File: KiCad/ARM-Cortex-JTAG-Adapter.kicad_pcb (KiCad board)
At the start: 2 copper layers, 36.1 x 30.5 mm, 4 parts, among them J1 I/O, J2 Power

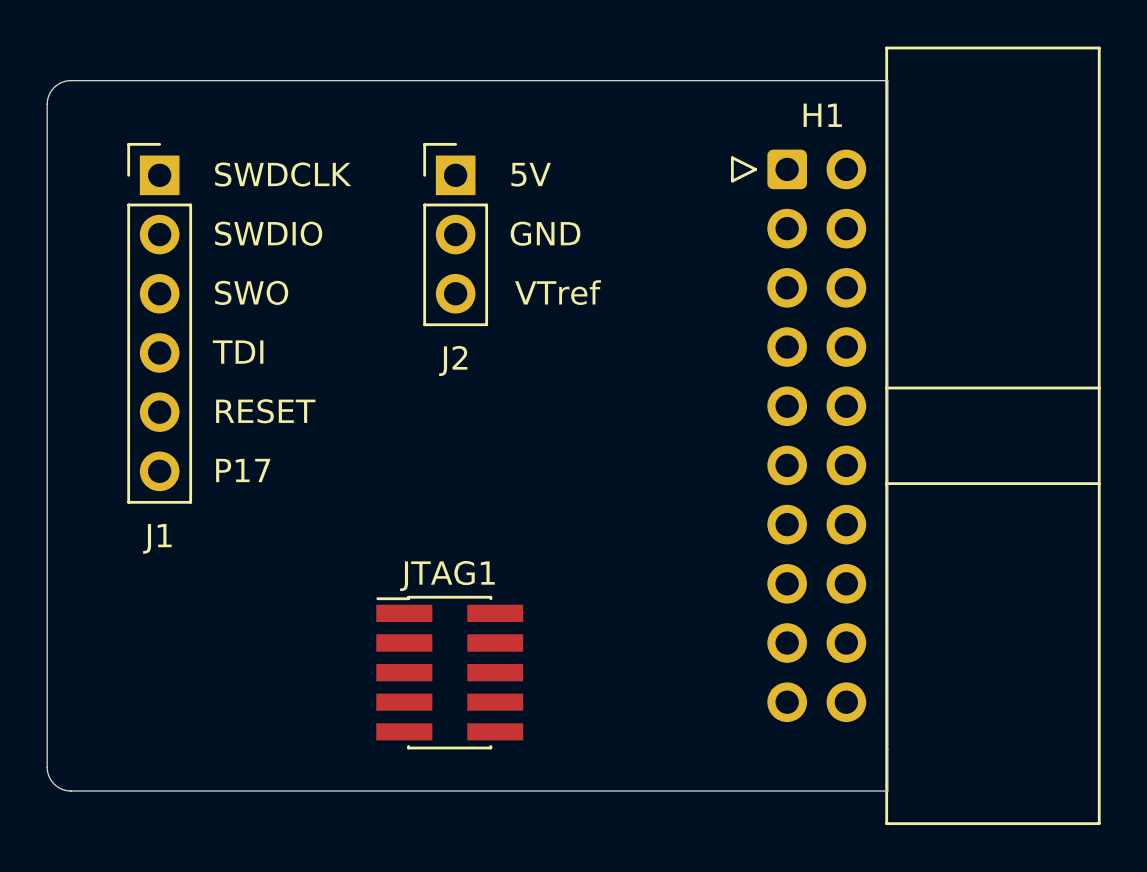
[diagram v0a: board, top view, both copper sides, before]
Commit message: Updating schematic and PCB layout.
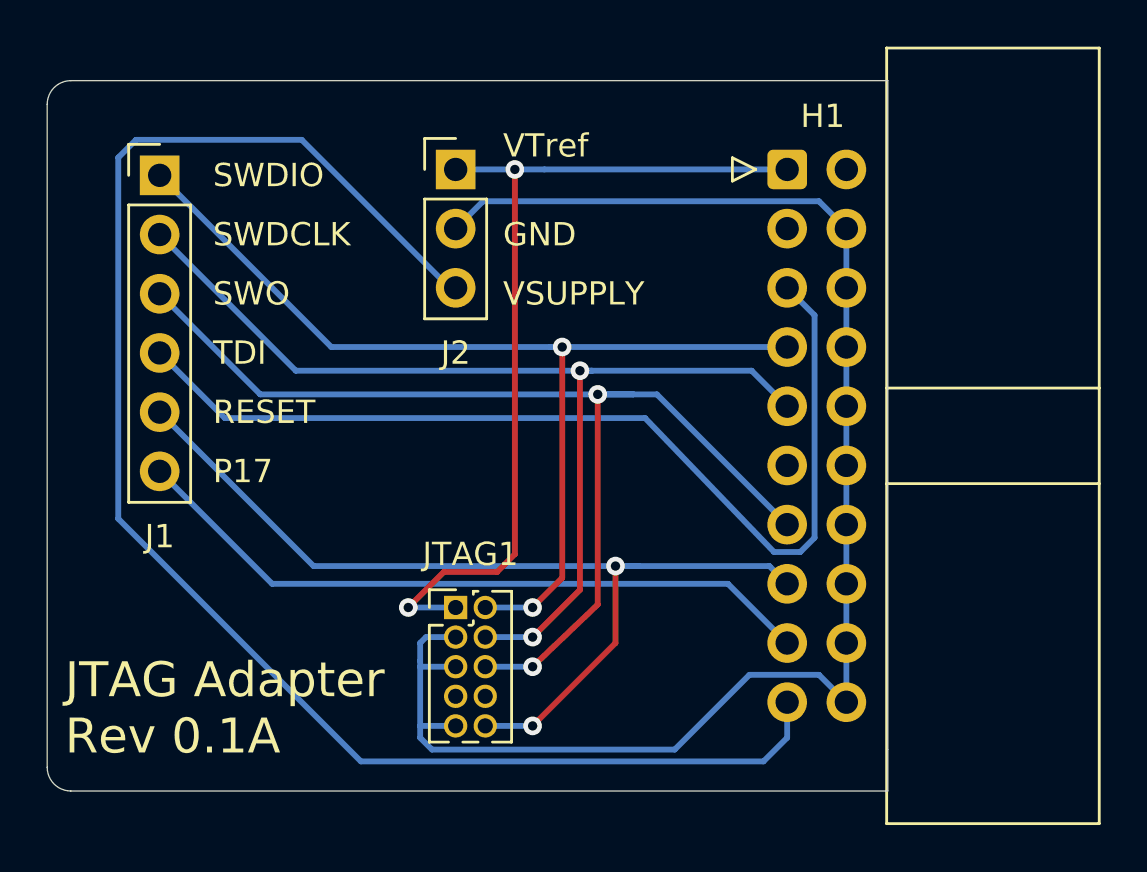
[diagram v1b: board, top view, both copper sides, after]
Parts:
- H1: value 2x10 IDC Header Connector -> IDC-Header_2x10_P2.54mm_Horizontal
- J1: value I/O -> Data
- JTAG1: footprint Connector_PinHeader_1.27mm:PinHeader_2x05_P1.27mm_Vertical_SMD -> Connector_PinHeader_1.27mm:PinHeader_2x05_P1.27mm_Vertical
- moved JTAG1 2.81 mm to (144.8, 129.5)
- moved J2 0.25 mm to (144.8, 110.7)
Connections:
- J1 pad 1: /SWDCLK -> /SWDIO
- J1 pad 2: /SWDIO -> /SWDCLK
- J2 pad 1: /5V -> /VTref
- J2 pad 3: /VTref -> /5V
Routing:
- net /5V: track 0.00 -> 68.0 mm
- net /GND: track 0.00 -> 67.1 mm
- net /SWO: track 0.00 -> 47.5 mm, vias 0 -> 2
- net /SWDCLK: track 0.00 -> 44.8 mm, vias 0 -> 2
- net /SWDIO: track 0.00 -> 43.7 mm, vias 0 -> 2
- net /TDI: track 0.00 -> 43.2 mm
- net /RESET: track 0.00 -> 41.1 mm, vias 0 -> 2
- net /VTref: track 0.00 -> 38.3 mm, vias 0 -> 2
- net /P17: track 0.00 -> 30.0 mm
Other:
- board text added: "JTAG Adapter Rev 0.1A"
- board text added: "VSUPPLY"
- board text removed: "5V"

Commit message: Revising schematic for optional TDI pin.
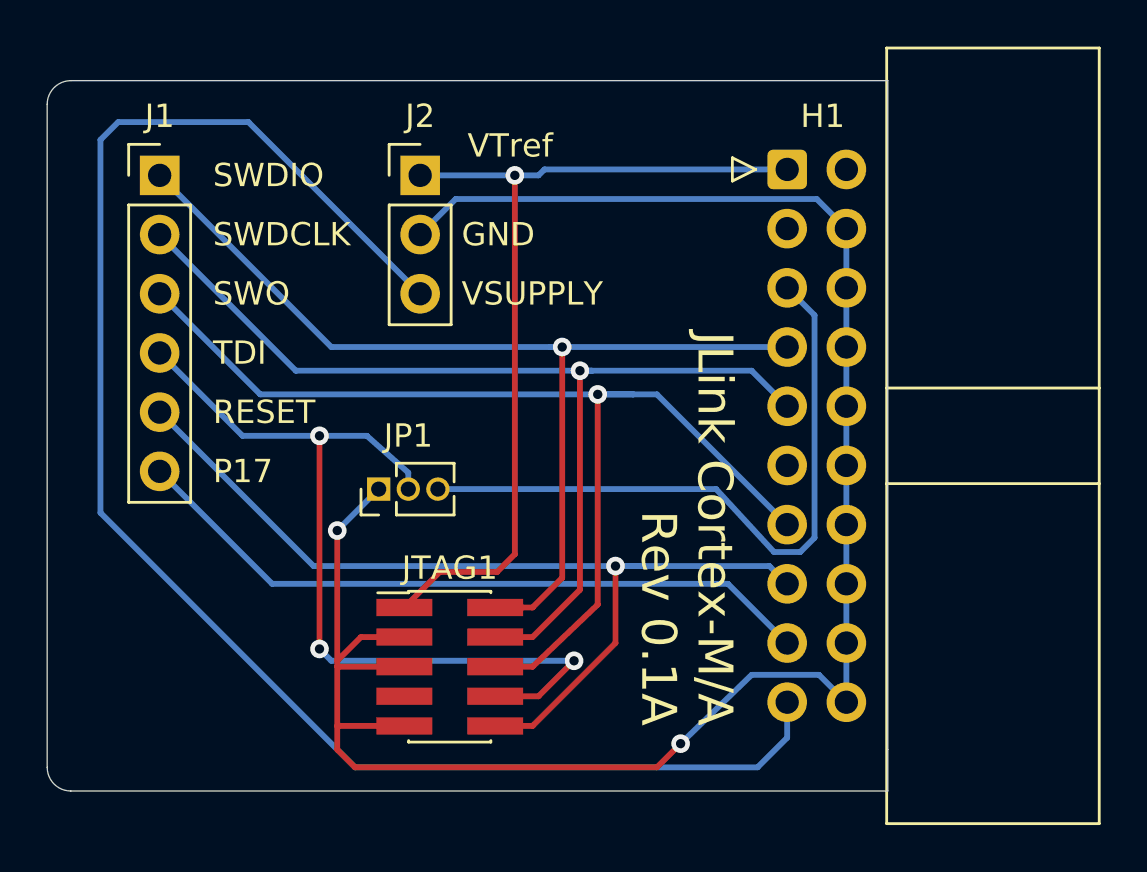
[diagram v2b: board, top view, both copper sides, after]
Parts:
- added JP1: M50-3530342, Connector_PinHeader_1.27mm:PinHeader_1x03_P1.27mm_Vertical, F.Cu at (141.5, 124.5)
- H1: value IDC-Header_2x10_P2.54mm_Horizontal -> SSW-110-02-T-D-RA
- JTAG1: value JTAG SWD -> FTSH-105-01-L-DV-007-K; footprint Connector_PinHeader_1.27mm:PinHeader_2x05_P1.27mm_Vertical -> Connector_PinHeader_1.27mm:PinHeader_2x05_P1.27mm_Vertical_SMD
- moved JTAG1 2.55 mm to (144.5, 132.1)
- moved J2 1.55 mm to (143.3, 111.0)
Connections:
- J1 pad 4: /TDI -> /TDI_IN
- JTAG1 pad 8: Net-(JTAG1-Pad8) -> /TDI_IN
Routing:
- net /TDI_IN: track 0.00 -> 37.7 mm, vias 0 -> 3
- net /GND: track 67.1 -> 85.2 mm, vias 0 -> 2
- net /TDI: track 43.2 -> 28.8 mm
- net /5V: track 68.0 -> 69.1 mm
- net /VTref: track 38.3 -> 37.8 mm, vias 2 -> 1
- net /SWO: track 47.5 -> 47.0 mm, vias 2 -> 1
- net /SWDIO: track 43.7 -> 43.3 mm, vias 2 -> 1
- net /SWDCLK: track 44.8 -> 44.4 mm, vias 2 -> 1
- net /RESET: track 41.1 -> 40.7 mm, vias 2 -> 1
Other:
- board text added: "JLink Cortex-M/A Rev 0.1A"
- board text removed: "JTAG Adapter Rev 0.1A"

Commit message: Adding labels to the TDI connector header.
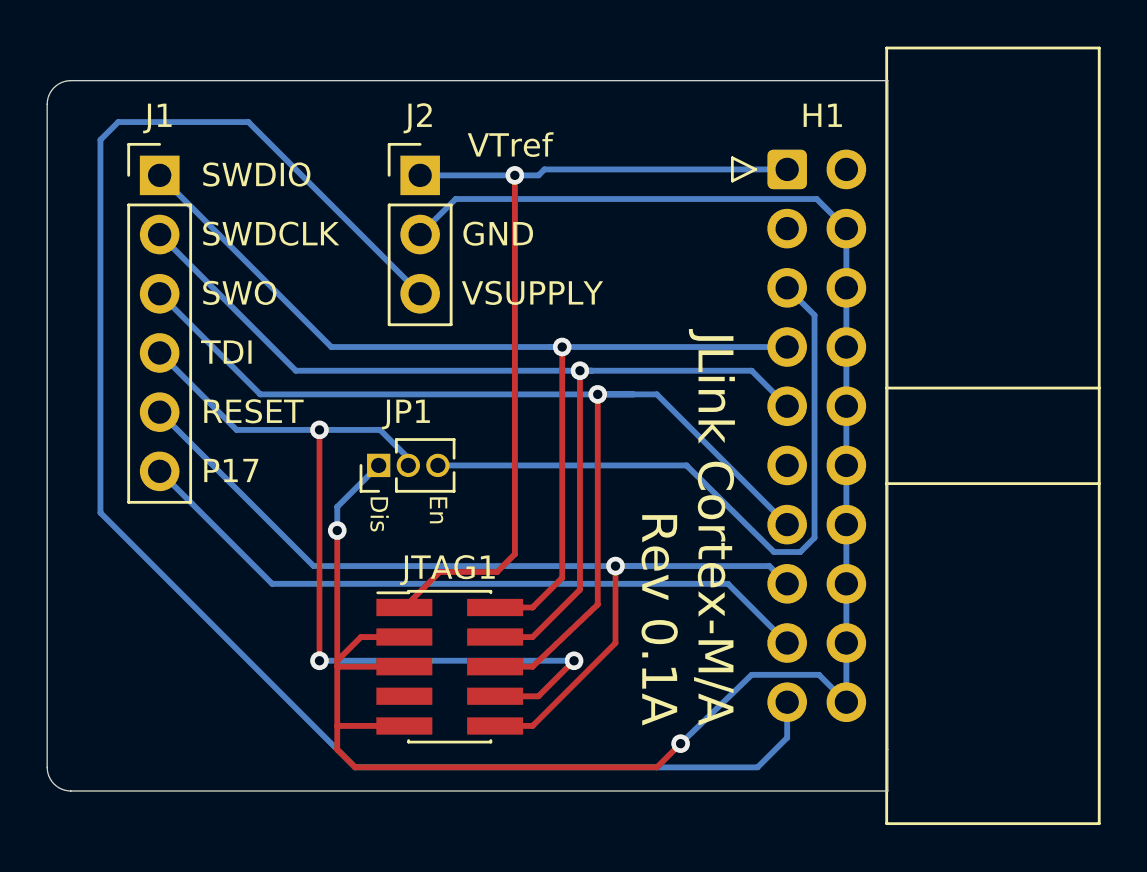
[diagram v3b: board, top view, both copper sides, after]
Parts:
- moved JP1 1.02 mm to (141.5, 123.4)
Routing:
- net /GND: track 85.2 -> 86.0 mm
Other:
- board text added: "Dis"
- board text added: "En"

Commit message: Updates.
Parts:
- H1: value SSW-110-02-T-D-RA -> 200-SSW11002TDRA
- JP1: value M50-3530342 -> 855-M50-3530342; footprint Connector_PinHeader_1.27mm:PinHeader_1x03_P1.27mm_Vertical -> Connector_PinHeader_2.54mm:PinHeader_1x02_P2.54mm_Vertical
- JTAG1: value FTSH-105-01-L-DV-007-K -> FTSH-105-01-L-DV-K; footprint Connector_PinHeader_1.27mm:PinHeader_2x05_P1.27mm_Vertical_SMD -> (Local):SAMTEC-FTSH-105-01-X-DV
- moved JP1 0.25 mm to (141.7, 123.4)
- turned JTAG1 to 270 degrees
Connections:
- JP1 pad 1: /GND -> /TDI_IN
- JP1 pad 2: /TDI_IN -> /TDI
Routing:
- net /GND: track 86.0 -> 76.9 mm, vias 2 -> 1
- net /TDI_IN: track 37.4 -> 36.2 mm
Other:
- board text removed: "Dis"
- board text removed: "En"
